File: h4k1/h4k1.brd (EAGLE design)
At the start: 250 x 80 mm, 198 parts, among them IC1 STM32F10XCXT6, J2 PJ-313D-AUDIO-JACK, J3 USB-AF10, K1 CHERRY-MX-LED, K10 CHERRY-MX, K11 CHERRY-MX, K12 CHERRY-MX, K13 CHERRY-MX, K14 CHERRY-MX, K15 CHERRY-MX, K16 CHERRY-MX, K17 CHERRY-MX-LED, K18 CHERRY-MX, K19 CHERRY-MX, K2 CHERRY-MX-LED, K20 CHERRY-MX, K21 CHERRY-MX, K22 CHERRY-MX, K23 CHERRY-MX, K24 CHERRY-MX, K25 CHERRY-MX-LED, K26 CHERRY-MX, K27 CHERRY-MX, K28 CHERRY-MX, K29 CHERRY-MX, K3 CHERRY-MX-LED, K30 CHERRY-MX, K31 CHERRY-MX, K32 CHERRY-MX, K33 CHERRY-MX-LED, K34 CHERRY-MX, K35 CHERRY-MX, K36 CHERRY-MX-LED, K37 CHERRY-MX-LED, K38 CHERRY-MX, K39 CHERRY-MX, K4 CHERRY-MX-LED, K40 CHERRY-MX-LED, K41 CHERRY-MX, K42 CHERRY-MX, K43 CHERRY-MX, K44 CHERRY-MX, K45 CHERRY-MX, K46 CHERRY-MX-LED, K5 CHERRY-MX-LED, K6 CHERRY-MX-LED, K65 EVQPUL02K, K66 EVQPUL02K, K67 K3-1280S-F2, K7 CHERRY-MX-LED, K8 CHERRY-MX-LED, K9 CHERRY-MX-LED, T1 DBG, U1 GL850G, U3 PCM2704CDB, X3 12MHz, X4 12MHz

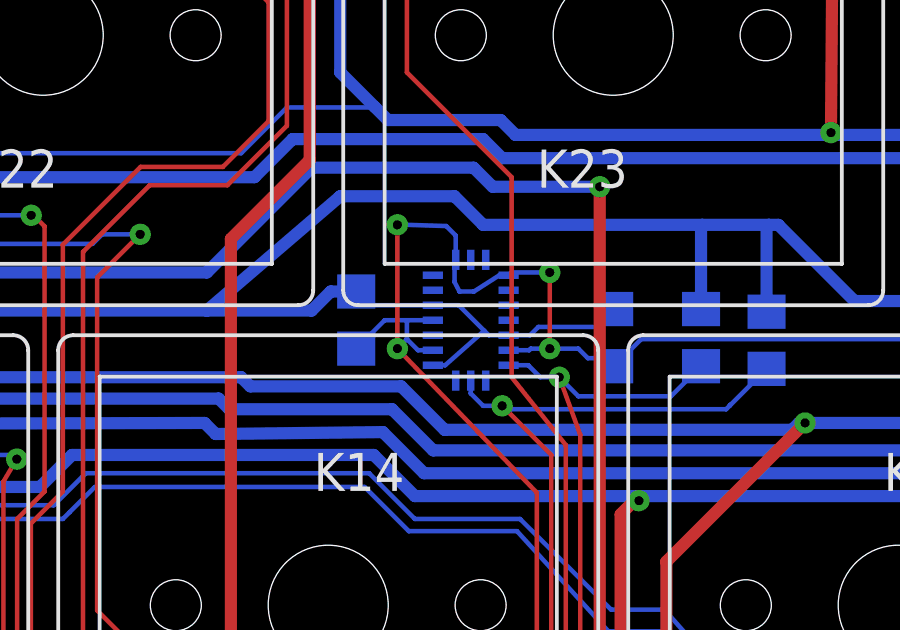
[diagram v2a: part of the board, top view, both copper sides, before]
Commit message: using hqc bmx055
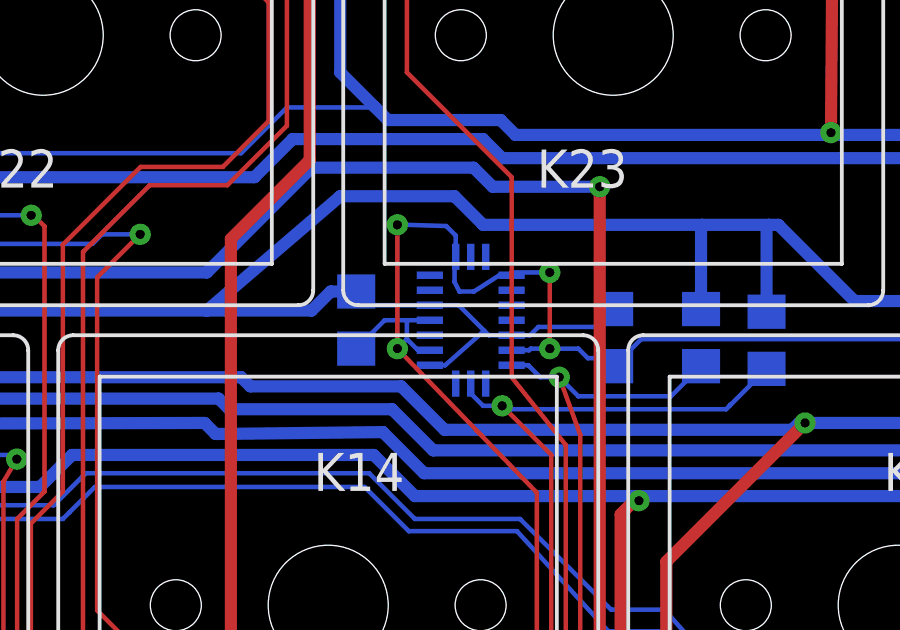
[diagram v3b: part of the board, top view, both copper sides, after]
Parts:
- U$4: device sensor:BMX055 -> hqc:BMX055
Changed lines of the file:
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@@
 <attribute name="VALUE" x="2.7" y="49.7458" size="1.27" layer="28" rot="MR180"/>
 </element>
-<element name="U$4" library="sensor" package="BMX055" value="BMX055" x="125" y="40" smashed="yes" rot="MR0">
+<element name="U$4" library="hqc" package="BMX055" value="BMX055" x="125" y="40" smashed="yes" rot="MR0">
 <attribute name="NAME" x="125.7092" y="35.5428" size="1.27" layer="26" rot="MR0"/>
 </element>
@@
 <wire x1="108.7882" y1="40.3225" x2="116.205" y2="40.3225" width="0.4064" layer="16"/>
 <wire x1="116.205" y1="40.3225" x2="119.6975" y2="40.3225" width="0.4064" layer="16"/>
-<wire x1="123.7375" y1="40.5" x2="121.6409" y2="40.5" width="0.1524" layer="16"/>
+<wire x1="123.6375" y1="40.5" x2="121.6409" y2="40.5" width="0.1524" layer="16"/>
 <wire x1="121.6409" y1="40.5" x2="121.1834" y2="40.9575" width="0.1524" layer="16"/>
-<wire x1="126.2625" y1="39.5" x2="126.9776" y2="39.5" width="0.1524" layer="16"/>
+<wire x1="126.3625" y1="39.5" x2="126.9776" y2="39.5" width="0.1524" layer="16"/>
 <wire x1="126.9776" y1="39.5" x2="127.254" y2="39.7764" width="0.1524" layer="16"/>
-<wire x1="123.7375" y1="40.5" x2="124.6" y2="40.5" width="0.1524" layer="16"/>
-<wire x1="126.2625" y1="39.5" x2="125.6" y2="39.5" width="0.1524" layer="16"/>
+<wire x1="123.6375" y1="40.5" x2="124.6" y2="40.5" width="0.1524" layer="16"/>
+<wire x1="126.3625" y1="39.5" x2="125.6" y2="39.5" width="0.1524" layer="16"/>
 <wire x1="125.6" y1="39.5" x2="125.4506" y2="39.6494" width="0.1524" layer="16"/>
 <wire x1="125.4506" y1="39.6494" x2="124.6" y2="40.5" width="0.1524" layer="16"/>
@@
 <wire x1="109.4825" y1="20.784" x2="109.4825" y2="21.2767" width="0.1524" layer="16"/>
 <wire x1="109.4825" y1="21.2767" x2="109.4232" y2="21.336" width="0.1524" layer="16"/>
-<wire x1="123.7375" y1="38.5" x2="124.1488" y2="38.5" width="0.1524" layer="16"/>
+<wire x1="123.6375" y1="38.5" x2="124.1488" y2="38.5" width="0.1524" layer="16"/>
 <wire x1="124.1488" y1="38.5" x2="125.4506" y2="39.6494" width="0.1524" layer="16"/>
 <wire x1="127.254" y1="39.7764" x2="129.1844" y2="39.7764" width="0.1524" layer="16"/>
@@
 <wire x1="77.7875" y1="42.8625" x2="78.79590625" y2="42.8625" width="0.4064" layer="16"/>
 <wire x1="78.79590625" y1="42.8625" x2="79.6544" y2="43.2181" width="0.4064" layer="16" curve="45"/>
-<wire x1="123.7375" y1="40" x2="122.8725" y2="40" width="0.1524" layer="16"/>
+<wire x1="123.6375" y1="40" x2="122.8725" y2="40" width="0.1524" layer="16"/>
 <wire x1="122.8725" y1="40" x2="122.1309" y2="40" width="0.1524" layer="16"/>
 <wire x1="122.1309" y1="40" x2="121.1834" y2="39.0525" width="0.1524" layer="16"/>
 <wire x1="129.2496" y1="39" x2="129.7813" y2="38.4683" width="0.1524" layer="16"/>
-<wire x1="123.7375" y1="39" x2="123.2425" y2="39" width="0.1524" layer="16"/>
+<wire x1="123.6375" y1="39" x2="123.2425" y2="39" width="0.1524" layer="16"/>
 <wire x1="123.2425" y1="39" x2="122.8725" y2="39.37" width="0.1524" layer="16"/>
 <wire x1="122.8725" y1="39.37" x2="122.8725" y2="40" width="0.1524" layer="16"/>
-<wire x1="126.2625" y1="41.5" x2="125.955" y2="41.5" width="0.1524" layer="16"/>
+<wire x1="126.3625" y1="41.5" x2="125.955" y2="41.5" width="0.1524" layer="16"/>
 <wire x1="125.955" y1="41.5" x2="125.1077" y2="40.9575" width="0.1524" layer="16"/>
 <wire x1="125.1077" y1="40.9575" x2="124.6251" y2="40.9575" width="0.1524" layer="16"/>
 <wire x1="124.6251" y1="40.9575" x2="124.46" y2="41.275" width="0.1524" layer="16"/>
 <wire x1="124.46" y1="41.275" x2="124.46" y2="41.9725" width="0.1524" layer="16"/>
-<wire x1="124.46" y1="41.9725" x2="124.5" y2="42.0125" width="0.1524" layer="16"/>
-<wire x1="126.2625" y1="39" x2="126.9475" y2="39" width="0.1524" layer="16"/>
+<wire x1="124.46" y1="41.9725" x2="124.5" y2="42.1125" width="0.1524" layer="16"/>
+<wire x1="126.3625" y1="39" x2="126.9475" y2="39" width="0.1524" layer="16"/>
 <wire x1="126.9475" y1="39" x2="127" y2="39.0525" width="0.1524" layer="16"/>
 <wire x1="127" y1="39.0525" x2="127.635" y2="39.0525" width="0.1524" layer="16"/>
@@
 <via x="127.635" y="41.5925" extent="1-16" drill="0.3048"/>
 <wire x1="127.635" y1="41.5925" x2="126.355" y2="41.5925" width="0.1524" layer="16"/>
-<wire x1="126.355" y1="41.5925" x2="126.2625" y2="41.5" width="0.1524" layer="16"/>
+<wire x1="126.355" y1="41.5925" x2="126.3625" y2="41.5" width="0.1524" layer="16"/>
 <wire x1="127.635" y1="39.0525" x2="128.5875" y2="39.0525" width="0.1524" layer="16"/>
 <wire x1="128.5875" y1="39.0525" x2="128.905" y2="38.735" width="0.1524" layer="16"/>
 <wire x1="128.905" y1="38.735" x2="129.5146" y2="38.735" width="0.1524" layer="16"/>
 <wire x1="129.5146" y1="38.735" x2="129.7813" y2="38.4683" width="0.1524" layer="16"/>
-<wire x1="124.5" y1="42.0125" x2="124.5" y2="42.8225" width="0.1524" layer="16"/>
+<wire x1="124.5" y1="42.1125" x2="124.5" y2="42.8225" width="0.1524" layer="16"/>
 <wire x1="124.5" y1="42.8225" x2="124.1825" y2="43.14" width="0.1524" layer="16"/>
 <wire x1="124.1825" y1="43.14" x2="122.8725" y2="43.18" width="0.1524" layer="16"/>
@@
 <contactref element="IC1" pad="45"/>
 <contactref element="R35" pad="P$1"/>
-<wire x1="125" y1="37.9875" x2="125" y2="37.56" width="0.1524" layer="16"/>
+<wire x1="125" y1="37.8875" x2="125" y2="37.56" width="0.1524" layer="16"/>
 <wire x1="125" y1="37.56" x2="125.4125" y2="37.1475" width="0.1524" layer="16"/>
 <wire x1="125.4125" y1="37.1475" x2="126.0475" y2="37.1475" width="0.1524" layer="16"/>
@@
 <wire x1="128.651" y1="36.1823" x2="127.9525" y2="38.1" width="0.1524" layer="1"/>
 <via x="127.9525" y="38.1" extent="1-16" drill="0.3048"/>
-<wire x1="126.2625" y1="38.5" x2="126.9175" y2="38.5" width="0.1524" layer="16"/>
+<wire x1="126.3625" y1="38.5" x2="126.9175" y2="38.5" width="0.1524" layer="16"/>
 <wire x1="126.9175" y1="38.5" x2="127.3175" y2="38.1" width="0.1524" layer="16"/>
 <wire x1="127.3175" y1="38.1" x2="127.9525" y2="38.1" width="0.1524" layer="16"/>

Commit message: update circuit
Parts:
- added U4: 74HC138, hqc:SSOP16-208MIL
- moved R40 140.1 mm to (166.6, 30.8), turned to 180 degrees
- moved U$2 41.9 mm to (-36.5, 17.2)
- moved U$3 36.1 mm to (-28.5, 33.2)
- moved D37 14.5 mm to (214.7, 36.9)
- moved D36 14.5 mm to (232.3, 36.3)
- moved D25 13.6 mm to (8.66, 74.7)
- moved D9 13.5 mm to (16.4, 36.7), turned to 0 degrees
- moved D46 8.19 mm to (232.7, 63.7), turned to 90 degrees
- moved J3 4.14 mm to (0.00, 32.1)
- moved K65 3.00 mm to (23.0, 72.2)
- moved K66 3.00 mm to (227.0, 72.2)
- moved D6 1.31 mm to (130.0, 17.6)
- moved D49 0.96 mm to (228.2, 67.9)
- moved R42 0.64 mm to (8.52, 8.51), turned to 0 degrees
- turned K25 to 0 degrees
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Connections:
- new net MCU_RX: IC1.43
- new net MCU_TX: IC1.42
- new net RS_A0: IC1.19, U4.P$1
- new net RS_A1: IC1.20, U4.P$2
- new net RS_A2: IC1.39, U4.P$3
- new net RS_EN: IC1.18, U4.P$6
- net GND: now also U4.P$4, U4.P$5, U4.P$8
- net KB_R1: now also U4.P$15; no longer IC1.18
- net KB_R2: now also U4.P$14; no longer IC1.19
- net KB_R3: now also U4.P$13; no longer IC1.20
- net KB_R4: now also U4.P$12; no longer IC1.39
- net KB_R5: now also U4.P$11; no longer IC1.40
- net KB_R6: now also U4.P$10; no longer IC1.41
- net KB_R7: now also U4.P$9; no longer IC1.42
- net N$76: now also IC1.40; no longer IC1.29
- net N$80: now also IC1.41; no longer IC1.30
- net N$81: now also IC1.28, R42.P$1; no longer IC1.31, R41.P$1
- net N$85: now also IC1.27, R41.P$1; no longer IC1.38, R42.P$1
- net VDD: now also U4.P$16
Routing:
- net KB_R7: track 304.0 -> 15.0 mm, vias 3 -> 0
- net N$85: track 127.3 -> 4.79 mm, vias 2 -> 1
- net LED_C1: track 257.8 -> 176.5 mm
- net GND: track 645.7 -> 578.6 mm, vias 30 -> 28
- net N$81: track 79.1 -> 16.7 mm, vias 2 -> 1
- net LED_C3: track 238.6 -> 178.0 mm, vias 7 -> 6
- net KB_R4: track 201.2 -> 141.2 mm, vias 2 -> 0
- net KB_R6: track 207.4 -> 150.8 mm, vias 4 -> 1
- net N$80: track 131.0 -> 77.0 mm, vias 2 -> 6
- net KB_R5: track 227.8 -> 174.1 mm, vias 4 -> 1
- net SWCLK: track 228.9 -> 175.4 mm, vias 4 -> 6
- net KB_R3: track 188.5 -> 140.7 mm, vias 2 -> 0
- net SWDIO: track 217.7 -> 182.8 mm, vias 4 -> 2
- net N$23: track 280.9 -> 311.9 mm, vias 13 -> 14
- net RS_A2: track 0.00 -> 29.3 mm, vias 0 -> 4
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
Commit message: layout 74138
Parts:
- moved R42 115.3 mm to (123.8, 12.9), turned to 270 degrees
- moved U$2 92.9 mm to (40.0, 70.0)
- moved U$3 79.6 mm to (49.0, 15.0)
- moved R41 60.7 mm to (98.2, 50.4), turned to 0 degrees
- moved D30 15.4 mm to (99.1, 65.4), turned to 180 degrees
- moved D22 1.38 mm to (101.4, 52.5)
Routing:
- net KB_R7: track 15.0 -> 263.7 mm, vias 0 -> 3
- net GND: track 578.6 -> 796.9 mm, vias 28 -> 32
- net KB_R5: track 174.1 -> 273.6 mm, vias 1 -> 4
- net KB_R6: track 150.8 -> 198.3 mm, vias 1 -> 3
- net N$85: track 4.79 -> 47.3 mm, vias 1 -> 2
- net VDD: track 318.0 -> 360.0 mm, vias 8 -> 11
- net KB_R4: track 141.2 -> 169.7 mm, vias 0 -> 2
- net KB_R2: track 147.2 -> 175.6 mm, vias 1 -> 2
- net KB_R1: track 302.1 -> 329.9 mm, vias 5 -> 6
- net KB_R3: track 140.7 -> 159.4 mm, vias 0 -> 1
- net LED_C2: track 115.6 -> 126.8 mm
- net LED_R2: track 373.8 -> 384.2 mm, vias 7 -> 8
- net N$81: track 16.7 -> 26.2 mm, vias 1 -> 2
- net N$58: track 3.67 -> 10.6 mm
- net N$74: track 36.3 -> 43.0 mm, vias 1 -> 2
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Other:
- board text added: ">H4K-v0.2 20170818<"
- board text removed: ">H4K-v0.1 20170731<"

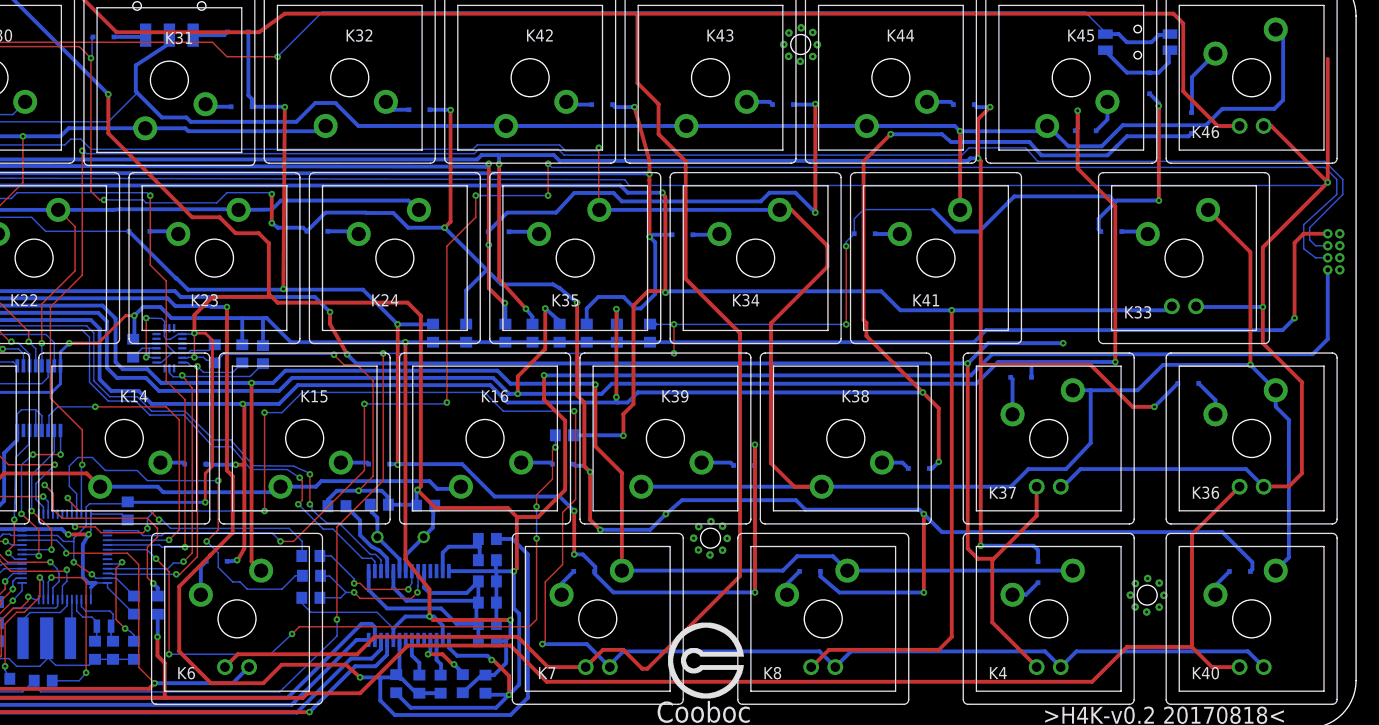
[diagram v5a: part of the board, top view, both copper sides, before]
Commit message: add serial port
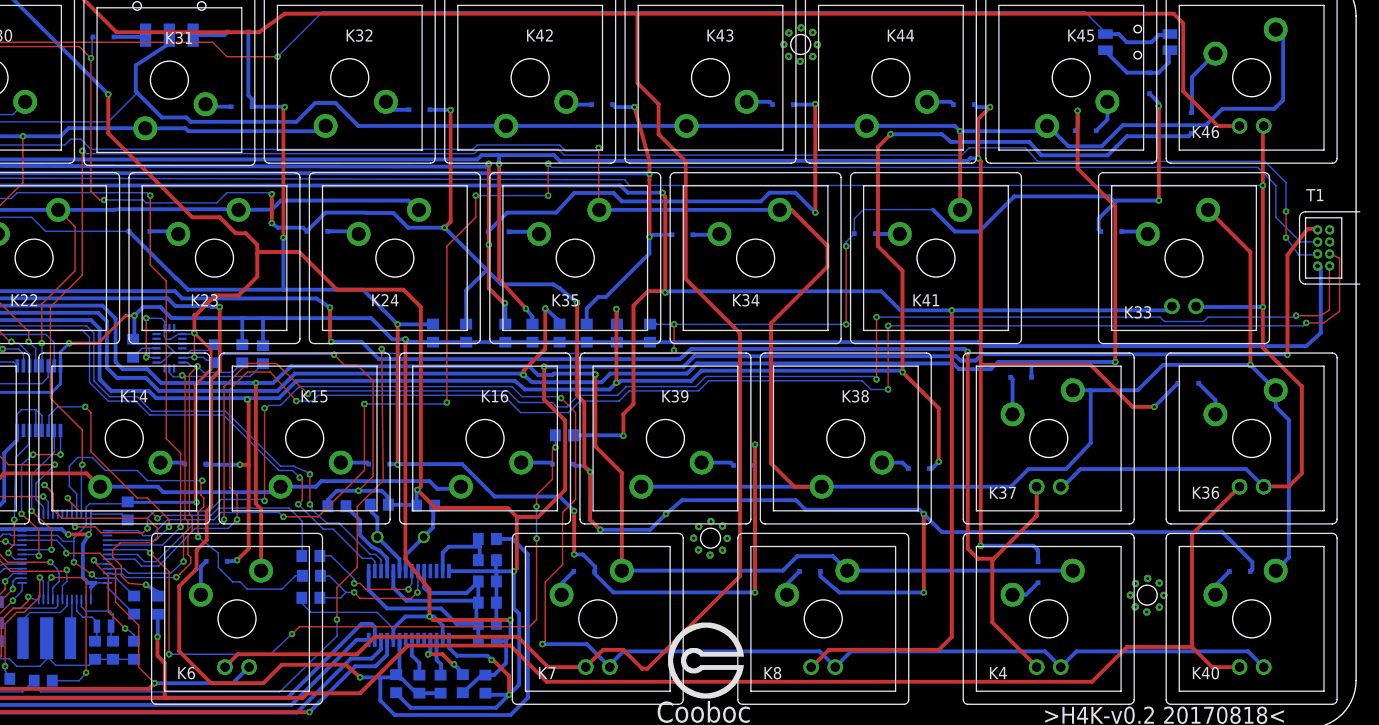
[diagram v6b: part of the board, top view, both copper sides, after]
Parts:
- moved T1 3.57 mm to (245.9, 48.7), flipped to the top, turned to 90 degrees
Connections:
- net MCU_RX: now also T1.P$2
- net MCU_TX: now also T1.P$1
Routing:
- net MCU_RX: track 0.00 -> 165.8 mm, vias 0 -> 5
- net MCU_TX: track 0.00 -> 161.2 mm, vias 0 -> 5
- net LED_C4: track 282.2 -> 255.7 mm
- net SWCLK: track 176.5 -> 166.7 mm
- net LED_R3: track 308.3 -> 299.6 mm, vias 7 -> 6
- net N$81: track 26.2 -> 32.3 mm
- net RS_A2: track 35.9 -> 29.9 mm
- net SWDIO: track 186.1 -> 180.4 mm, vias 2 -> 4
- net N$15: track 310.6 -> 306.0 mm
- net N$5: track 341.4 -> 337.0 mm
- net GND: track 796.9 -> 799.3 mm, vias 32 -> 33
- net N$13: track 273.6 -> 271.2 mm
- net N$72: track 30.7 -> 32.9 mm
- net N$76: track 88.1 -> 86.0 mm
- net VDD: track 360.0 -> 358.1 mm, vias 11 -> 10
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
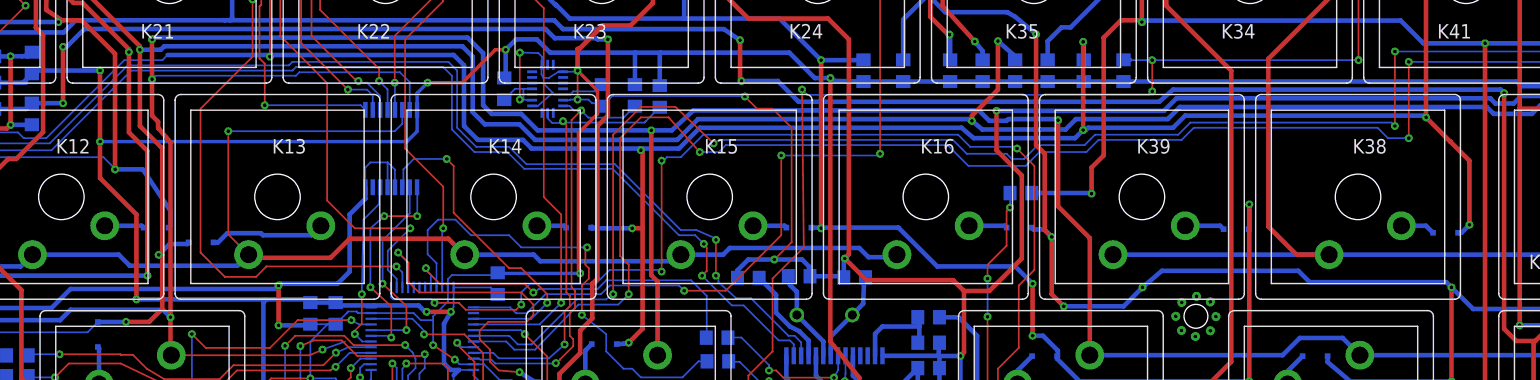
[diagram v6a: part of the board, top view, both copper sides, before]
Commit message: add vbus sense circuit
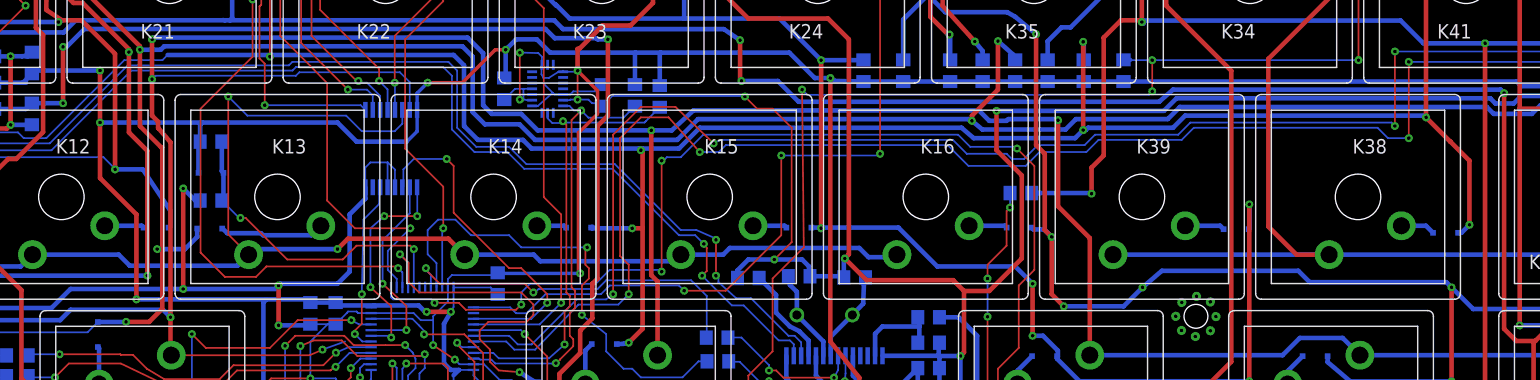
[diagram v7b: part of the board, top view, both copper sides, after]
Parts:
- added C36: 1uF, hqc:0805
- added D51: (no value), hqc-basic:SOD-323
- added R43: 1.5k, hqc:0805
- moved D13 1.44 mm to (95.3, 27.7)
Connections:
- new net PWR_SENSE: C36.P$2, D51.P$1, IC1.29, R43.P$2
- net GND: now also C36.P$1
- net VDD: now also D51.P$2, R43.P$1
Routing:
- net PWR_SENSE: track 0.00 -> 28.3 mm, vias 0 -> 2
- net GND: track 799.3 -> 810.1 mm, vias 33 -> 35
- net VDD: track 358.1 -> 363.4 mm
- net KB_R2: track 175.6 -> 179.7 mm, vias 2 -> 3
- net N$13: track 271.2 -> 272.9 mm
- net N$27: track 11.0 -> 10.1 mm
